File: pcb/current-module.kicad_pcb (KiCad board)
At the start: 4 copper layers, 50 x 50 mm, 128 parts, among them J2 SWD Header, SW1 SKRPABE010, U1 STM32C051G8Ux, U2 A1324LLHLT-T, U3 A1324LLHLT-T, U4 TLV9064, Y1 ECS-480-10-37B2-RWN-TR

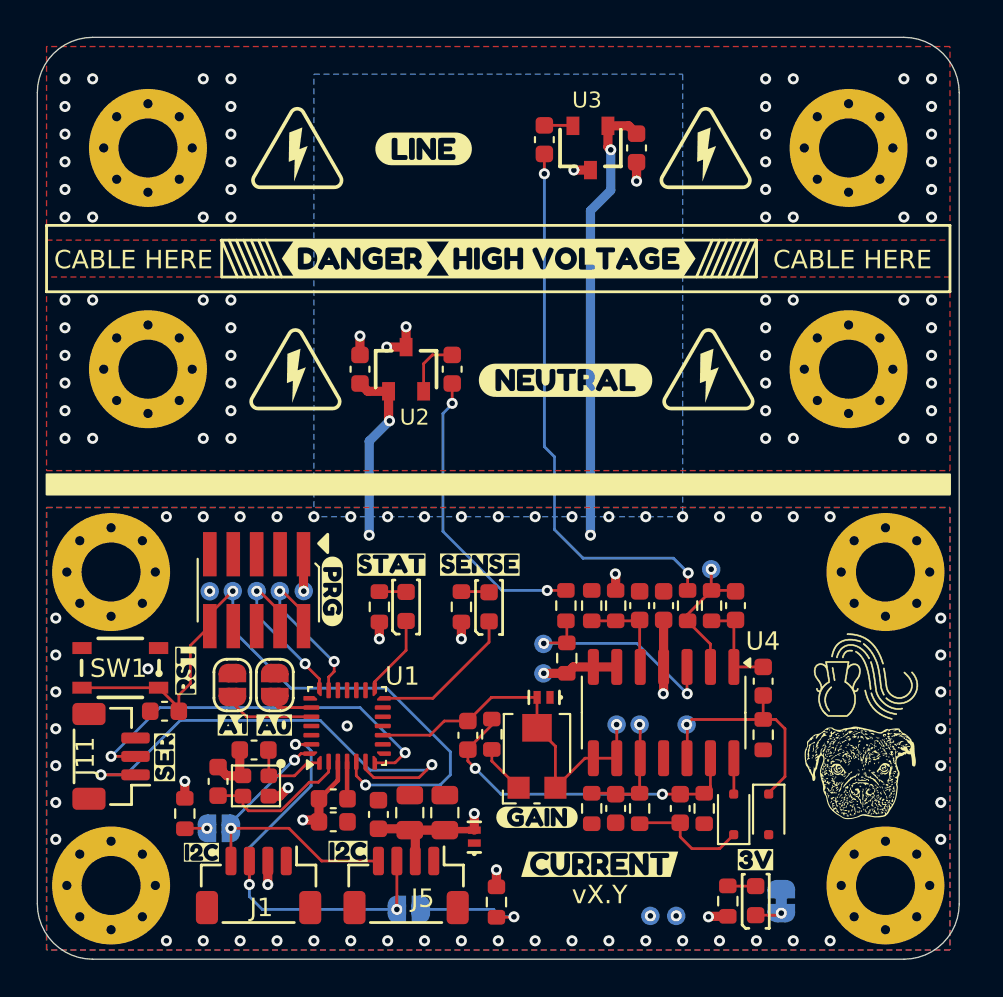
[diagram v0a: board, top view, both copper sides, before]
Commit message: Removed AC input via copper
Testing revealed sending AC through copper did not trigger device. Removed ability to send AC through the PCB.
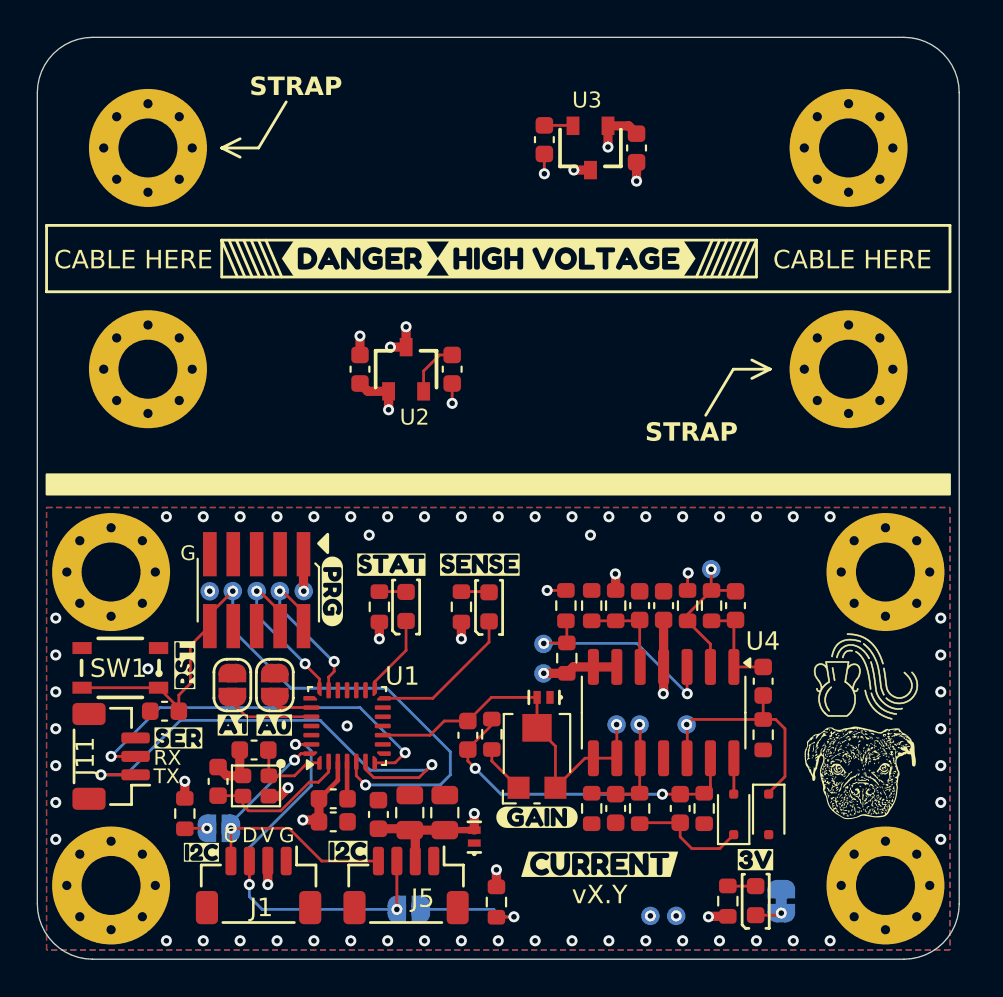
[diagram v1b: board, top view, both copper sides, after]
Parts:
- removed SYM1, SYM2, SYM3, SYM4, SYM5, SYM6, SYM7, SYM8: ~, CRGM Symbols:HIGH-VOLTAGE-5MM
- removed the kibuzzard-68F7E620 at (67.5, 112.5)
- removed the kibuzzard-68F7E62B at (78.7, 112.5)
- removed kibuzzard-6AA9ECA7: G***, kibuzzard-6AA9ECA7
- removed kibuzzard-6AA9ECB3: G***, kibuzzard-6AA9ECB3
- moved kibuzzard-6AAB5003 1.29 mm to (57.6, 138.0), turned to 0 degrees
- moved kibuzzard-6AAB4A0C 0.30 mm to (58.0, 134.1)
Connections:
- H5 pad 1: /Power/Line -> unconnected-(H5-Pad1)_7
- H6 pad 1: /Power/Line -> unconnected-(H6-Pad1)_5
- H7 pad 1: /Power/Neutral -> unconnected-(H7-Pad1)
- H8 pad 1: /Power/Neutral -> unconnected-(H8-Pad1)_6
- U1 pad 11: IO2 -> unconnected-(U1-PA5-Pad11)
- U1 pad 12: IO3 -> unconnected-(U1-PA6-Pad12)
- U1 pad 13: IO4 -> unconnected-(U1-PA7-Pad13)
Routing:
- net /Power/Neutral: vias 32 -> 0
- net /Power/Line: vias 32 -> 0
- removed copper zone on F.Cu, net /Power/Line
- removed copper zone on In1.Cu, net /Power/Line
- removed copper zone on F.Cu, net /Power/Neutral
- removed copper zone on In1.Cu, net /Power/Neutral
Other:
- board text added: "C"
- board text added: "D"
- board text added: "G"
- board text added: "RX"
- board text added: "STRAP"
- board text added: "TX"
- board text added: "V"
